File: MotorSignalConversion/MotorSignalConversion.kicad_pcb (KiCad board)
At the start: 2 copper layers, 100 x 84.7 mm, 22 parts, among them J1 Conn_01x06_MountingPin, J2 Conn_01x02, J3 Conn_01x06_MountingPin, J4 Conn_01x04, U1 SC0915, U2 MCP4725xxx-xCH, U3 MCP4725xxx-xCH, U4 LM324

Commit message: pcb revision 1 done
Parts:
- added G***: LOGO, Footprints:LeopardPawFootprint, F.Cu at (227.0, 60.0)
- added G***: LOGO, LOGO, F.Cu at (218.0, 60.0)
- added R7: 200K, Resistor_SMD:R_0805_2012Metric, F.Cu at (200.0, 107.5)
- added U5: LSF0102DCUR, Package_SO:VSSOP-8_2.3x2mm_P0.5mm, F.Cu at (193.6, 111.8)
- moved R6 19.1 mm to (214.1, 102.5)
- moved J2 17.5 mm to (227.5, 130.0), turned to 180 degrees
- moved J4 17.5 mm to (210.0, 129.2), turned to 180 degrees
- moved R1 11.2 mm to (169.1, 57.5)
- moved R2 10.3 mm to (168.4, 65.0)
- moved U4 3.54 mm to (212.5, 112.5)
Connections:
- J1 pad 4: /RefSpeed -> /SpeedLeft
- J2 pad 1: /0V -> /GND
- J2 pad 2: /0V -> /12V
- J3 pad 4: /RefSpeed -> /SpeedRight
- U1 pad 40: unconnected-(U1-VBUS-Pad40) -> /5V_OUT
- U4 pad 4: /0V -> /12V
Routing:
- net /3V3_OUT: track 0.00 -> 237.2 mm, vias 0 -> 9
- net /I2C SCL: track 0.00 -> 172.9 mm, vias 0 -> 2
- net /I2C SDA: track 0.00 -> 156.2 mm, vias 0 -> 3
- net /Enable: track 0.00 -> 117.6 mm, vias 0 -> 2
- net /Brake: track 0.00 -> 107.7 mm, vias 0 -> 4
- net /VOUT2: track 0.00 -> 80.1 mm, vias 0 -> 4
- net /5V_OUT: track 0.00 -> 79.4 mm
- net /SpeedLeft: track 0.00 -> 75.9 mm, vias 0 -> 2
- net /VOUT1: track 0.00 -> 75.6 mm, vias 0 -> 4
- net Net-(U4A--): track 0.00 -> 48.6 mm, vias 0 -> 2
- net /SpeedReadRegulatedR: track 0.00 -> 47.0 mm, vias 0 -> 2
- net /SpeedRight: track 0.00 -> 45.7 mm, vias 0 -> 2
- net /DirectionL: track 0.00 -> 43.0 mm, vias 0 -> 2
- net /12V: track 0.00 -> 42.9 mm, vias 0 -> 2
- net /DirectionR: track 0.00 -> 42.2 mm, vias 0 -> 2
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- added copper zone on B.Cu, net /GND
- added copper zone on F.Cu, net /GND
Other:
- board text added: "Assembly Number:"
- board text added: "Board Part Number:"
- board text added: "By Eren Tekbaş"
- board text added: "Electrical and Computer Engineering"
- board text added: "Made in USA"
- board text added: "Rev v1.0"
- board text added: "Serial Number:"

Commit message: added the manufacturer numbers, ready to export a 3d models
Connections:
- U2 pad 6: unconnected-(U2-A0-Pad6) -> /GND

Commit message: Added board part number
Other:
- board text added: "Board Part Number: 5"
- board text removed: "Board Part Number:"
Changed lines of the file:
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@@
 		(tags "connector JST PH vertical")
 		(property "Reference" "J2"
-			(at 0 5 360)
+			(at 0 5 0)
 			(layer "F.SilkS")
 			(effects
@@
 		)
 		(property "Value" "Conn_01x02"
-			(at 0 4.45 360)
+			(at 0 4.45 0)
 			(layer "F.Fab")
 			(effects
@@
 		)
 		(fp_text user "${REFERENCE}"
-			(at 0 -1 360)
+			(at 0 -1 0)
 			(layer "F.Fab")
 			(effects
@@
 		(tags "connector JST PH vertical")
 		(property "Reference" "J4"
-			(at 0 4.25 360)
+			(at 0 4.25 0)
 			(layer "F.SilkS")
 			(effects
@@
 		)
 		(property "Value" "Conn_01x04"
-			(at 0 4.45 360)
+			(at 0 4.45 0)
 			(layer "F.Fab")
 			(effects
@@
 		)
 		(fp_text user "${REFERENCE}"
-			(at 0 -1 360)
+			(at 0 -1 0)
 			(layer "F.Fab")
 			(effects
@@
 		(layer "Edge.Cuts")
 	)
-	(gr_text "Board Part Number:"
+	(gr_text "Board Part Number: 5"
 		(at 235 116 0)
 		(layer "B.SilkS")

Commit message: added the schematic for the battery circuit
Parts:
- removed J4: Conn_01x04, Connector_JST:JST_PH_B4B-PH-SM4-TB_1x04-1MP_P2.00mm_Vertical
- added J5: Conn_01x02, Connector_JST:JST_PH_B2B-PH-SM4-TB_1x02-1MP_P2.00mm_Vertical, F.Cu at (210.9, 130.5)
- added R10: 820K, Resistor_SMD:R_0805_2012Metric, F.Cu at (216.7, 85.0)
- added R11: 10K, Resistor_SMD:R_0805_2012Metric, F.Cu at (216.6, 90.0)
- added R8: 10K, Resistor_SMD:R_0805_2012Metric, F.Cu at (236.6, 87.5)
- added R9: 91K, Resistor_SMD:R_0805_2012Metric, F.Cu at (235.9, 70.0)
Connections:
- U1 pad 34: unconnected-(U1-GP28-Pad34) -> /BatteryLevelRegulated
- U4 pad 10: (no net) -> Net-(U4C-+)
- U4 pad 8: (no net) -> /BatteryLevelRegulated
- U4 pad 9: (no net) -> Net-(U4C--)
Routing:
- net /I2C SCL: track 172.9 -> 19.0 mm, vias 2 -> 1
- net /I2C SDA: track 156.2 -> 21.8 mm, vias 3 -> 2
- net /BatteryLevelRegulated: track 0.00 -> 107.3 mm, vias 0 -> 4
- net /BatteryLevelUnregulated: track 0.00 -> 93.4 mm, vias 0 -> 2
- net Net-(U4C--): track 0.00 -> 64.3 mm
- net /3V3_OUT: track 237.2 -> 197.3 mm, vias 9 -> 6
- net Net-(U4C-+): track 0.00 -> 5.79 mm
- net /GND: track 9.01 -> 8.68 mm, vias 4 -> 3

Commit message: revised PCB design, added text for connectors
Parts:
- moved J5 0.50 mm to (210.9, 130.0)
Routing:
- net Net-(U4C-+): track 5.79 -> 32.0 mm, vias 0 -> 2
- net /5V_OUT: track 79.4 -> 80.4 mm
- net /GND: track 8.68 -> 9.48 mm, vias 3 -> 4
- net /I2C SCL: vias 1 -> 0
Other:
- board text added: "Rev v2.0"
- board text added: "battery voltage level"
- board text added: "left motor controller"
- board text added: "op-amp power supply"
- board text added: "right motor controller"

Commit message: revised based on feedback
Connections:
- R1 pad 2: Net-(U1-GP5) -> /I2C SCL
- R2 pad 2: Net-(U1-GP4) -> /I2C SDA
- U1 pad 6: Net-(U1-GP4) -> /I2C SDA
- U1 pad 7: Net-(U1-GP5) -> /I2C SCL
- U4 pad 11: /0V -> /GND
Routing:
- net Net-(U1-GP5): track 21.4 -> 0.00 mm, vias 2 -> 0
- net /I2C SCL: track 19.0 -> 40.4 mm, vias 0 -> 2
- net Net-(U1-GP4): track 16.4 -> 0.00 mm
- net /I2C SDA: track 21.8 -> 38.3 mm
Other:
- board text added: "Rev v2.1"
- board text removed: "Rev v2.0"

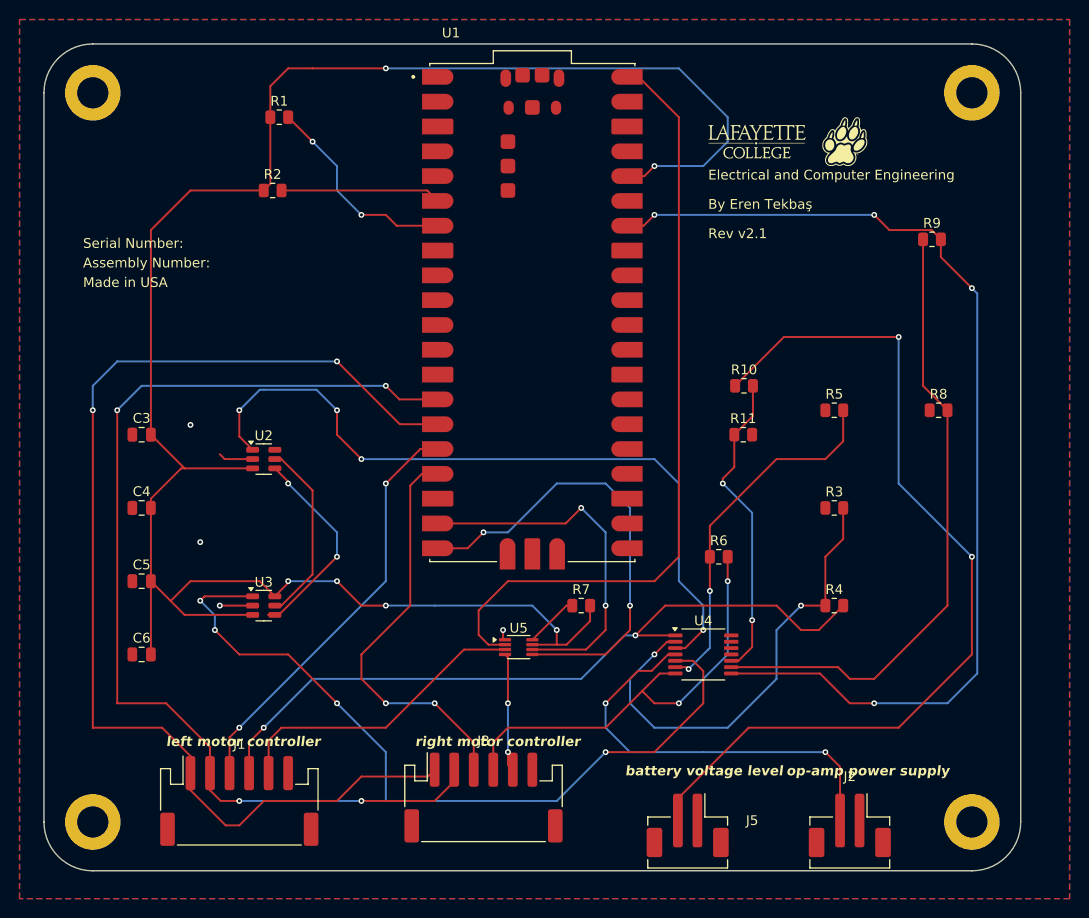
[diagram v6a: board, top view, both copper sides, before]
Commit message: fixed the issue with resistors for i2c
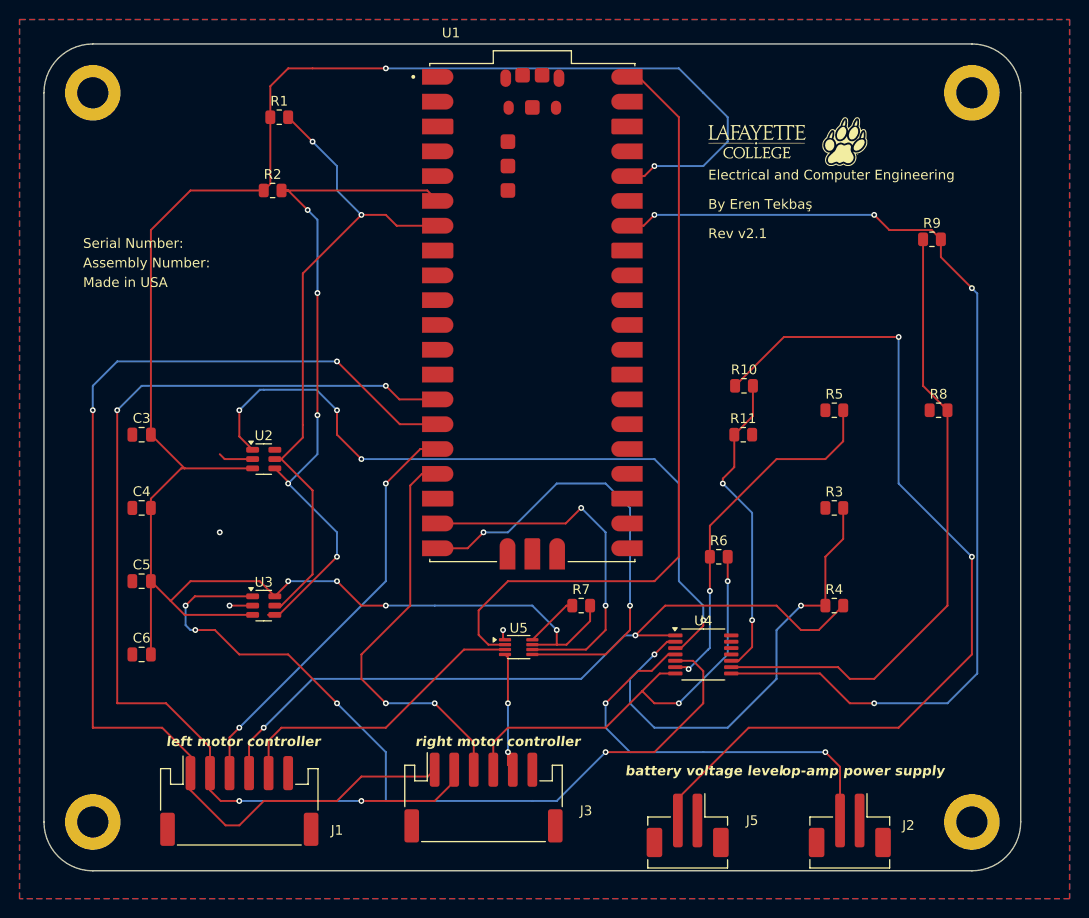
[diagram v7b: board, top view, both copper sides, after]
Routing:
- net /I2C SDA: track 38.3 -> 71.4 mm, vias 2 -> 5
- net /I2C SCL: track 40.4 -> 68.7 mm
- net /VOUT2: track 80.1 -> 83.4 mm
- net /GND: track 9.48 -> 8.48 mm, vias 4 -> 3

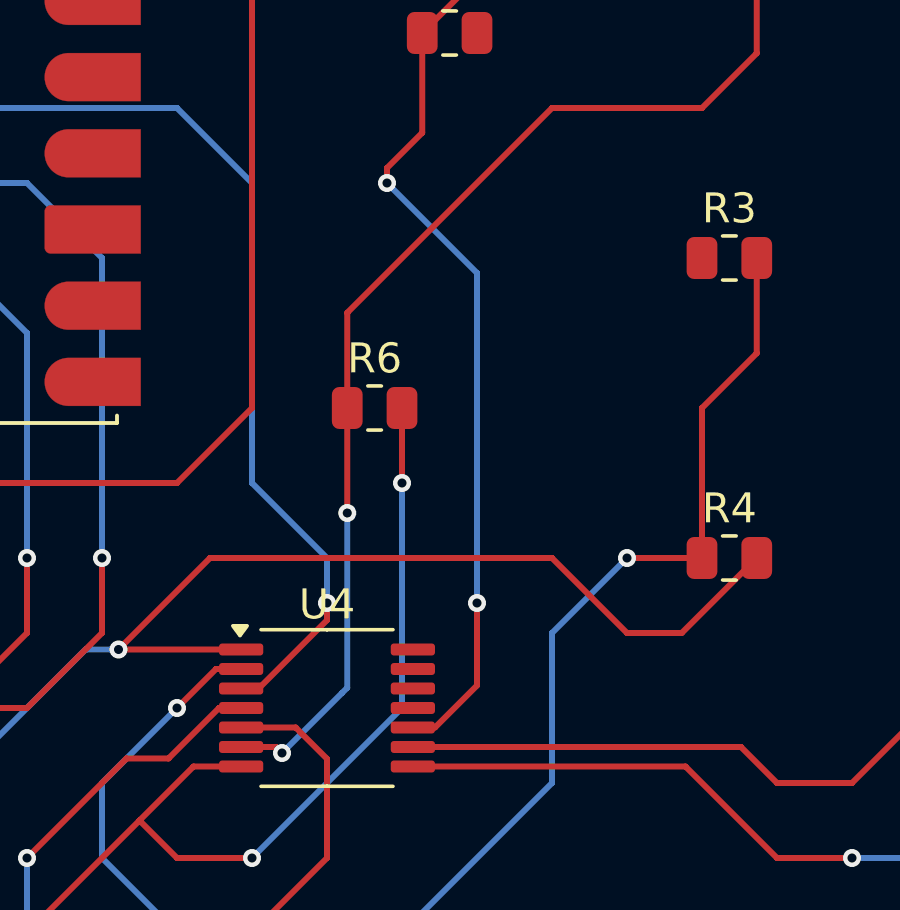
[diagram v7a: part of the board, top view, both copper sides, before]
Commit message: fixed opamp gnd issue
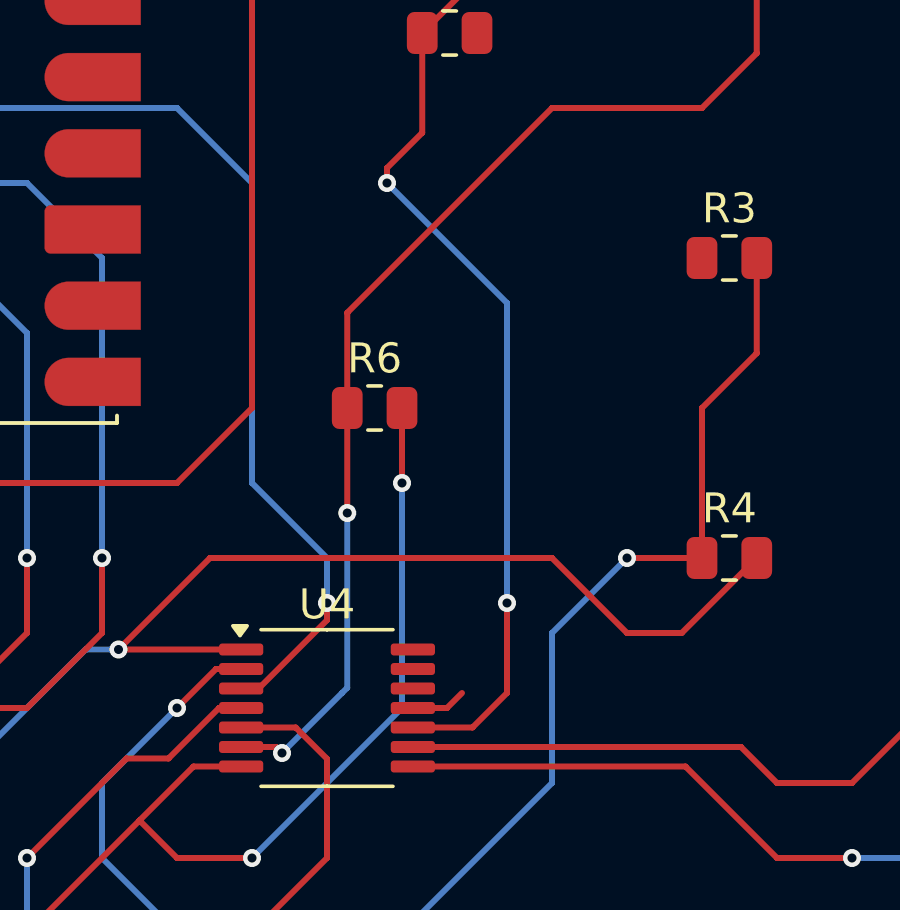
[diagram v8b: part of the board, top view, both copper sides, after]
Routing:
- net /GND: track 8.48 -> 10.3 mm
- net Net-(U4C-+): track 32.0 -> 33.5 mm
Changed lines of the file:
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@@
+	)
+	(segment
+		(start 215.3625 112.5)
+		(end 216.5 112.5)
+		(width 0.2)
+		(layer "F.Cu")
+		(net 2)
+	)
+	(segment
+		(start 216.5 112.5)
+		(end 217 112)
+		(width 0.2)
+		(layer "F.Cu")
+		(net 2)
 	)
 	(segment
@@
 	)
 	(segment
-		(start 217.5 111.749999)
-		(end 217.5 109)
-		(width 0.2)
-		(layer "F.Cu")
-		(net 68)
-	)
-	(segment
-		(start 216.099999 113.15)
-		(end 217.5 111.749999)
-		(width 0.2)
-		(layer "F.Cu")
-		(net 68)
-	)
-	(segment
-		(start 215.3625 113.15)
-		(end 216.099999 113.15)
-		(width 0.2)
-		(layer "F.Cu")
-		(net 68)
-	)
-	(segment
 		(start 217.5825 88.0925)
 		(end 215.675 90)
@@
 	)
 	(segment
+		(start 217.35 113.15)
+		(end 215.3625 113.15)
+		(width 0.2)
+		(layer "F.Cu")
+		(net 68)
+	)
+	(segment
+		(start 218.5 112)
+		(end 217.35 113.15)
+		(width 0.2)
+		(layer "F.Cu")
+		(net 68)
+	)
+	(segment
 		(start 217.5825 85)
 		(end 217.5825 88.0925)
@@
 		(net 68)
 	)
+	(segment
+		(start 218.5 109)
+		(end 218.5 112)
+		(width 0.2)
+		(layer "F.Cu")
+		(net 68)
+	)
 	(via
 		(at 214.5 95)
@@
 	)
 	(via
-		(at 217.5 109)
+		(at 218.5 109)
 		(size 0.6)
 		(drill 0.3)
@@
 	)
 	(segment
-		(start 217.5 98)
+		(start 218.5 109)
+		(end 218.5 99)
+		(width 0.2)
+		(layer "B.Cu")
+		(net 68)
+	)
+	(segment
+		(start 218.5 99)
 		(end 214.5 95)
 		(width 0.2)
 		(layer "B.Cu")
-		(net 68)
-	)
-	(segment
-		(start 217.5 109)
-		(end 217.5 98)
-		(width 0.2)
-		(layer "B.Cu")
